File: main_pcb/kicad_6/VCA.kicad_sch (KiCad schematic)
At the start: 22 parts, among them J501 aux_AM_in, U4 TL072, U9 SSI2162

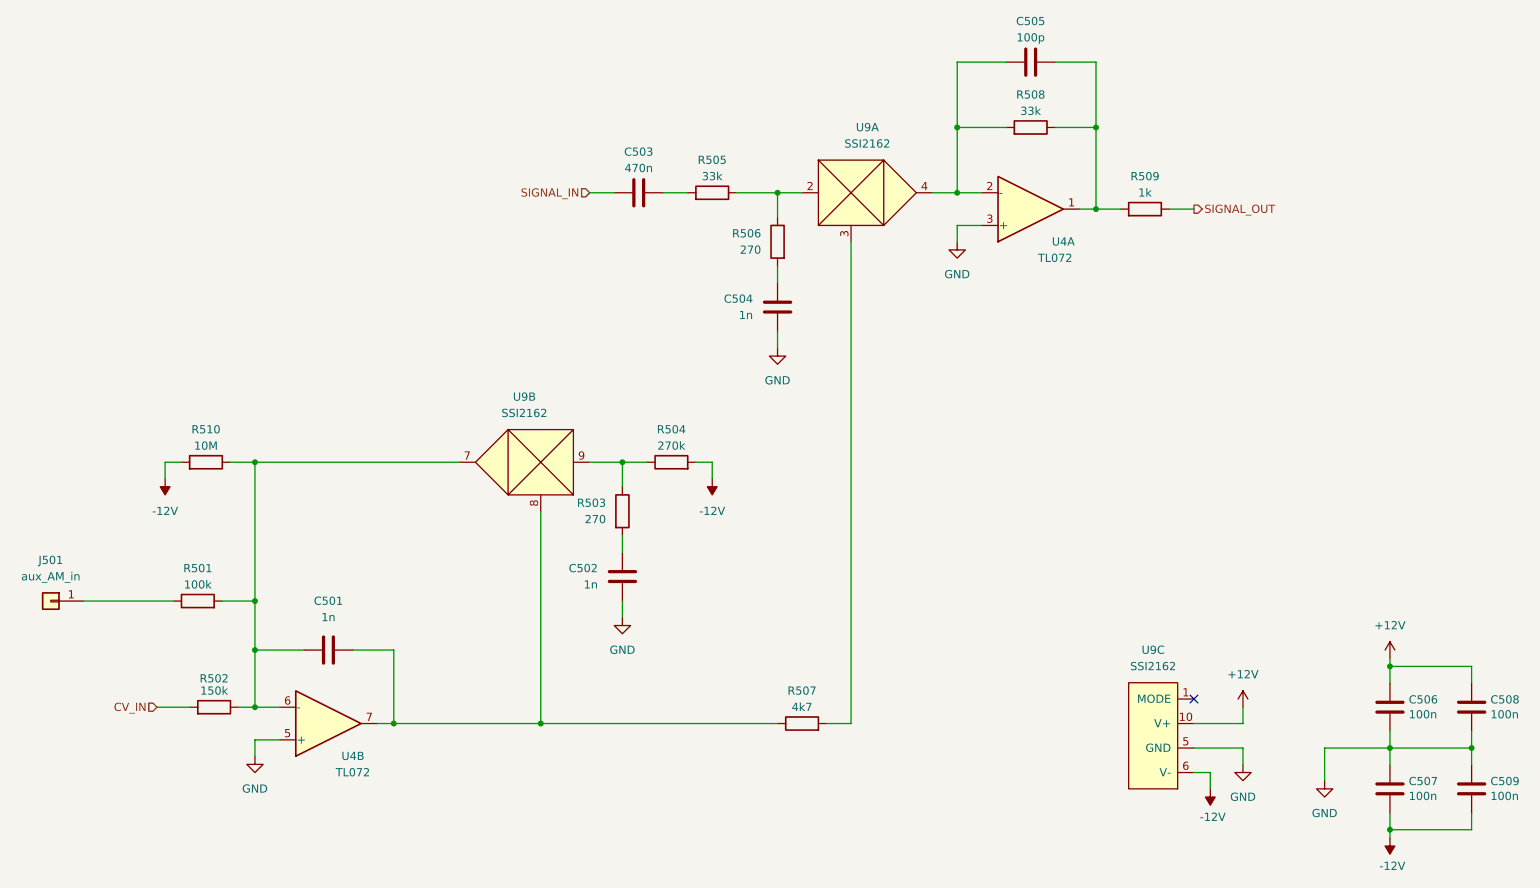
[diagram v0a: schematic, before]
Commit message: Update rev 0.1, fix VCA tails, add local 2v5 regs, change some pot footprints
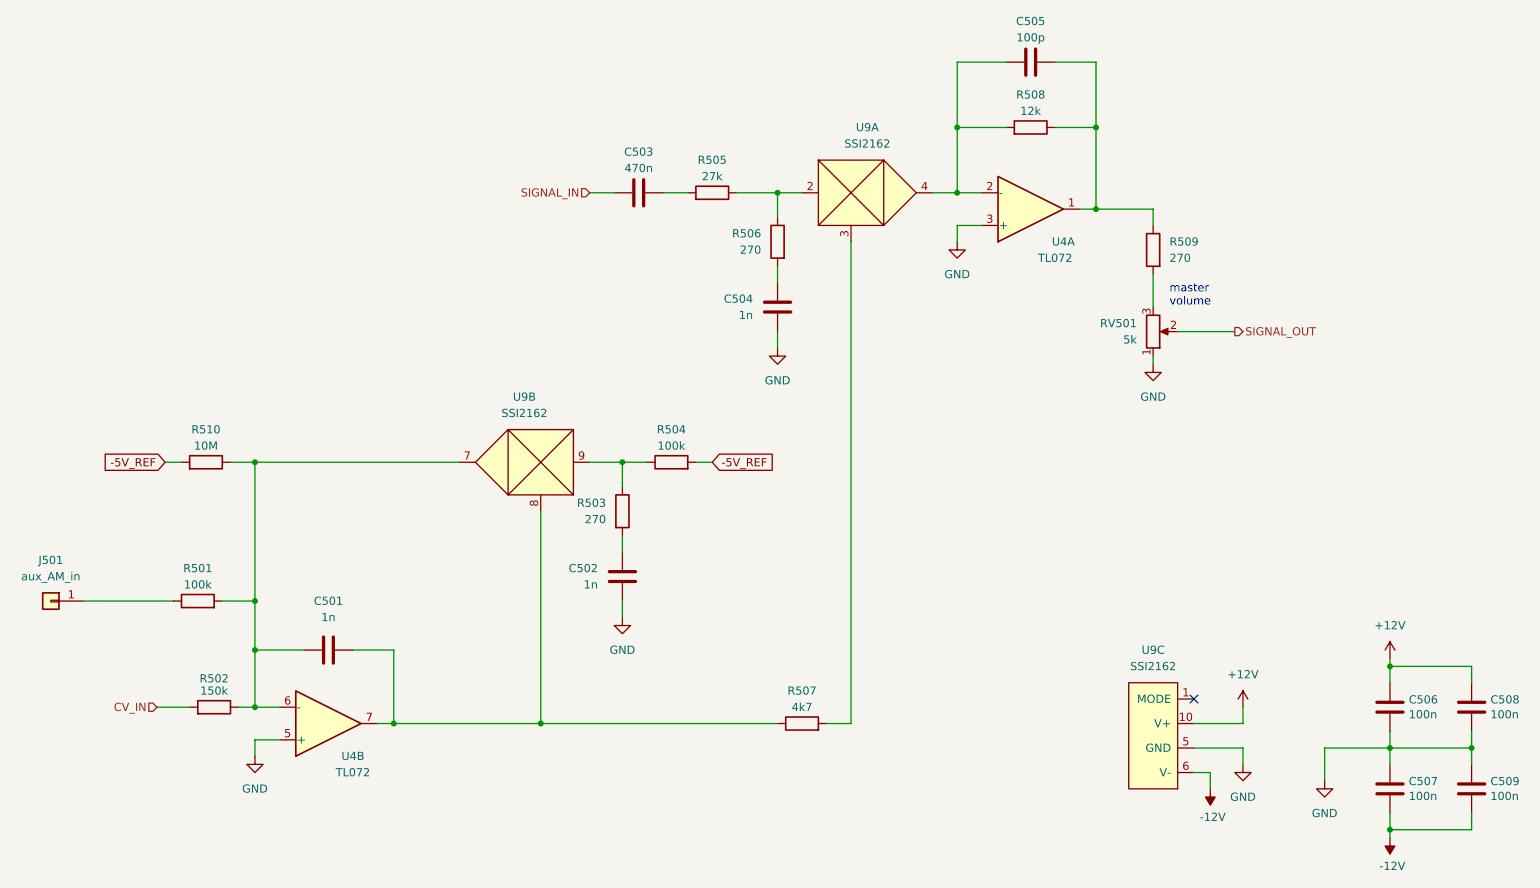
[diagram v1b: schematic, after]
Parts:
- added RV501: 5k, custom_footprints:Bourns_PTV09, symbol Device:R_Potentiometer
- J501: now left out of the parts list
- R504: value 270k -> 100k
- R505: value 33k -> 27k
- R508: value 33k -> 12k
- R509: value 1k -> 270
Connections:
- net -12V: no longer R504.2, R510.2
- net GND: now also RV501.1
- net SIGNAL_OUT: now also RV501.2; no longer R509.1
- net at C505.1, R508.1, U4.1: now also R509.1; no longer R509.2
- new net: R509.2, RV501.3
- new net -5V_REF: R504.2, R510.2
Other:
- note added: "master volume"
- moved on the sheet: R509
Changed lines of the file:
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@@
   (title_block
     (title "Micro-Pico Tiny Monosynth")
-    (date "2022-08-18")
+    (date "2022-08-28")
     (rev "0.1")
     (comment 1 "creativecommons.org/licences/by/4.0")
@@
     (stroke (width 0) (type default) (color 0 0 0 0))
   )
+  (wire (pts (xy 151.13 97.79) (xy 148.59 97.79))
+    (stroke (width 0) (type default) (color 0 0 0 0))
+  )
   (wire (pts (xy 74.93 119.38) (xy 80.01 119.38))
     (stroke (width 0) (type default) (color 0 0 0 0))
@@
     (stroke (width 0) (type default) (color 0 0 0 0))
   )
+  (wire (pts (xy 219.71 68.58) (xy 219.71 73.66))
+    (stroke (width 0) (type default) (color 0 0 0 0))
+  )
   (wire (pts (xy 137.16 97.79) (xy 140.97 97.79))
     (stroke (width 0) (type default) (color 0 0 0 0))
@@
     (stroke (width 0) (type default) (color 0 0 0 0))
   )
-  (wire (pts (xy 66.04 100.33) (xy 66.04 97.79))
-    (stroke (width 0) (type default) (color 0 0 0 0))
-  )
   (wire (pts (xy 143.51 55.88) (xy 147.32 55.88))
     (stroke (width 0) (type default) (color 0 0 0 0))
@@
     (stroke (width 0) (type default) (color 0 0 0 0))
   )
+  (wire (pts (xy 219.71 81.28) (xy 219.71 82.55))
+    (stroke (width 0) (type default) (color 0 0 0 0))
+  )
   (wire (pts (xy 137.16 101.6) (xy 137.16 97.79))
     (stroke (width 0) (type default) (color 0 0 0 0))
@@
     (stroke (width 0) (type default) (color 0 0 0 0))
   )
+  (wire (pts (xy 223.52 77.47) (xy 232.41 77.47))
+    (stroke (width 0) (type default) (color 0 0 0 0))
+  )
   (wire (pts (xy 246.38 147.32) (xy 246.38 142.24))
     (stroke (width 0) (type default) (color 0 0 0 0))
@@
     (stroke (width 0) (type default) (color 0 0 0 0))
   )
-  (wire (pts (xy 151.13 97.79) (xy 148.59 97.79))
-    (stroke (width 0) (type default) (color 0 0 0 0))
-  )
   (wire (pts (xy 226.06 142.24) (xy 233.68 142.24))
     (stroke (width 0) (type default) (color 0 0 0 0))
@@
     (stroke (width 0) (type default) (color 0 0 0 0))
   )
-  (wire (pts (xy 222.25 58.42) (xy 226.06 58.42))
-    (stroke (width 0) (type default) (color 0 0 0 0))
-  )
   (wire (pts (xy 210.82 58.42) (xy 208.28 58.42))
     (stroke (width 0) (type default) (color 0 0 0 0))
   )
-  (wire (pts (xy 214.63 58.42) (xy 210.82 58.42))
+  (wire (pts (xy 210.82 58.42) (xy 219.71 58.42))
     (stroke (width 0) (type default) (color 0 0 0 0))
   )
@@
     (stroke (width 0) (type default) (color 0 0 0 0))
   )
+  (wire (pts (xy 219.71 58.42) (xy 219.71 60.96))
+    (stroke (width 0) (type default) (color 0 0 0 0))
+  )
   (wire (pts (xy 269.24 132.08) (xy 269.24 129.54))
     (stroke (width 0) (type default) (color 0 0 0 0))
@@
     (stroke (width 0) (type default) (color 0 0 0 0))
   )
-  (wire (pts (xy 151.13 100.33) (xy 151.13 97.79))
-    (stroke (width 0) (type default) (color 0 0 0 0))
-  )
   (wire (pts (xy 124.46 138.43) (xy 161.29 138.43))
     (stroke (width 0) (type default) (color 0 0 0 0))
@@
     (stroke (width 0) (type default) (color 0 0 0 0))
   )
-  (hierarchical_label "SIGNAL_OUT" (shape output) (at 226.06 58.42 0)
+  (text "master\nvolume" (at 222.25 73.66 0)
+    (effects (font (size 1.27 1.27)) (justify left bottom))
+  )
+  (global_label "-5V_REF" (shape input) (at 66.04 97.79 180) (fields_autoplaced)
+    (effects (font (size 1.27 1.27)) (justify right))
+    (property "Intersheet References" "${INTERSHEET_REFS}" (id 0) (at 55.2812 97.8694 0)
+      (effects (font (size 1.27 1.27)) (justify right) hide)
+    )
+  )
+  (global_label "-5V_REF" (shape input) (at 151.13 97.79 0) (fields_autoplaced)
+    (effects (font (size 1.27 1.27)) (justify left))
+    (property "Intersheet References" "${INTERSHEET_REFS}" (id 0) (at 161.8888 97.7106 0)
+      (effects (font (size 1.27 1.27)) (justify left) hide)
+    )
+  )
+  (hierarchical_label "SIGNAL_OUT" (shape output) (at 232.41 77.47 0)
     (effects (font (size 1.27 1.27)) (justify left))
   )
@@
     (in_bom yes) (on_board yes)
     (property "Reference" "R504" (id 0) (at 144.78 92.71 90))
-    (property "Value" "270k" (id 1) (at 144.78 95.25 90))
+    (property "Value" "100k" (id 1) (at 144.78 95.25 90))
     (property "Footprint" "Resistor_SMD:R_0603_1608Metric" (id 2) (at 144.78 99.568 90)
       (effects (font (size 1.27 1.27)) hide)
@@
   )
   (symbol (lib_id "Connector_Generic:Conn_01x01") (at 48.26 119.38 0) (mirror y) (unit 1)
-    (in_bom yes) (on_board yes) (fields_autoplaced)
+    (in_bom no) (on_board yes) (fields_autoplaced)
     (property "Reference" "J501" (id 0) (at 48.26 113.03 0))
     (property "Value" "aux_AM_in" (id 1) (at 48.26 115.57 0))
@@
     (pin "1")
   )
+  (symbol (lib_id "Device:R_Potentiometer") (at 219.71 77.47 0) (mirror x) (unit 1)
+    (in_bom yes) (on_board yes) (fields_autoplaced)
+    (property "Reference" "RV501" (id 0) (at 217.17 76.1999 0)
+      (effects (font (size 1.27 1.27)) (justify right))
+    )
+    (property "Value" "5k" (id 1) (at 217.17 78.7399 0)
+      (effects (font (size 1.27 1.27)) (justify right))
+    )
+    (property "Footprint" "custom_footprints:Bourns_PTV09" (id 2) (at 219.71 77.47 0)
+      (effects (font (size 1.27 1.27)) hide)
+    )
+    (property "Datasheet" "~" (id 3) (at 219.71 77.47 0)
+      (effects (font (size 1.27 1.27)) hide)
+    )
+    (pin "1")
+    (pin "2")
+    (pin "3")
+  )
   (symbol (lib_id "Device:R") (at 165.1 138.43 90) (unit 1)
     (in_bom yes) (on_board yes)
@@
     (pin "1")
   )
+  (symbol (lib_id "power:GND") (at 219.71 82.55 0) (unit 1)
+    (in_bom yes) (on_board yes) (fields_autoplaced)
+    (property "Reference" "#PWR0513" (id 0) (at 219.71 88.9 0)
+      (effects (font (size 1.27 1.27)) hide)
+    )
+    (property "Value" "GND" (id 1) (at 219.71 87.63 0))
+    (property "Footprint" "" (id 2) (at 219.71 82.55 0)
+      (effects (font (size 1.27 1.27)) hide)
+    )
+    (property "Datasheet" "" (id 3) (at 219.71 82.55 0)
+      (effects (font (size 1.27 1.27)) hide)
+    )
+    (pin "1")
+  )
   (symbol (lib_id "power:GND") (at 189.23 63.5 0) (mirror y) (unit 1)
     (in_bom yes) (on_board yes) (fields_autoplaced)
@@
     (pin "1")
     (pin "2")
-  )
-  (symbol (lib_id "power:-12V") (at 151.13 100.33 0) (mirror x) (unit 1)
-    (in_bom yes) (on_board yes) (fields_autoplaced)
-    (property "Reference" "#PWR0504" (id 0) (at 151.13 102.87 0)
-      (effects (font (size 1.27 1.27)) hide)
-    )
-    (property "Value" "-12V" (id 1) (at 151.13 105.41 0))
-    (property "Footprint" "" (id 2) (at 151.13 100.33 0)
-      (effects (font (size 1.27 1.27)) hide)
-    )
-    (property "Datasheet" "" (id 3) (at 151.13 100.33 0)
-      (effects (font (size 1.27 1.27)) hide)
-    )
-    (pin "1")
-  )
-  (symbol (lib_id "power:-12V") (at 66.04 100.33 180) (unit 1)
-    (in_bom yes) (on_board yes) (fields_autoplaced)
-    (property "Reference" "#PWR0501" (id 0) (at 66.04 102.87 0)
-      (effects (font (size 1.27 1.27)) hide)
-    )
-    (property "Value" "-12V" (id 1) (at 66.04 105.41 0))
-    (property "Footprint" "" (id 2) (at 66.04 100.33 0)
-      (effects (font (size 1.27 1.27)) hide)
-    )
-    (property "Datasheet" "" (id 3) (at 66.04 100.33 0)
-      (effects (font (size 1.27 1.27)) hide)
-    )
-    (pin "1")
   )
   (symbol (lib_id "Device:C") (at 91.44 127 270) (mirror x) (unit 1)
@@
     (in_bom yes) (on_board yes)
     (property "Reference" "R505" (id 0) (at 151.13 50.8 90))
-    (property "Value" "33k" (id 1) (at 151.13 53.34 90))
+    (property "Value" "27k" (id 1) (at 151.13 53.34 90))
     (property "Footprint" "Resistor_SMD:R_0603_1608Metric" (id 2) (at 151.13 57.658 90)
       (effects (font (size 1.27 1.27)) hide)
@@
     (pin "2")
   )
-  (symbol (lib_id "Device:R") (at 218.44 58.42 270) (mirror x) (unit 1)
-    (in_bom yes) (on_board yes)
-    (property "Reference" "R509" (id 0) (at 218.44 53.34 90))
-    (property "Value" "1k" (id 1) (at 218.44 55.88 90))
-    (property "Footprint" "Resistor_SMD:R_0603_1608Metric" (id 2) (at 218.44 60.198 90)
-      (effects (font (size 1.27 1.27)) hide)
-    )
-    (property "Datasheet" "~" (id 3) (at 218.44 58.42 0)
+  (symbol (lib_id "Device:R") (at 219.71 64.77 0) (mirror y) (unit 1)
+    (in_bom yes) (on_board yes) (fields_autoplaced)
+    (property "Reference" "R509" (id 0) (at 222.25 63.4999 0)
+      (effects (font (size 1.27 1.27)) (justify right))
+    )
+    (property "Value" "270" (id 1) (at 222.25 66.0399 0)
+      (effects (font (size 1.27 1.27)) (justify right))
+    )
+    (property "Footprint" "Resistor_SMD:R_0603_1608Metric" (id 2) (at 221.488 64.77 90)
+      (effects (font (size 1.27 1.27)) hide)
+    )
+    (property "Datasheet" "~" (id 3) (at 219.71 64.77 0)
       (effects (font (size 1.27 1.27)) hide)
     )
@@
     (in_bom yes) (on_board yes)
     (property "Reference" "R508" (id 0) (at 200.66 40.64 90))
-    (property "Value" "33k" (id 1) (at 200.66 43.18 90))
+    (property "Value" "12k" (id 1) (at 200.66 43.18 90))
     (property "Footprint" "Resistor_SMD:R_0603_1608Metric" (id 2) (at 200.66 47.498 90)
       (effects (font (size 1.27 1.27)) hide)

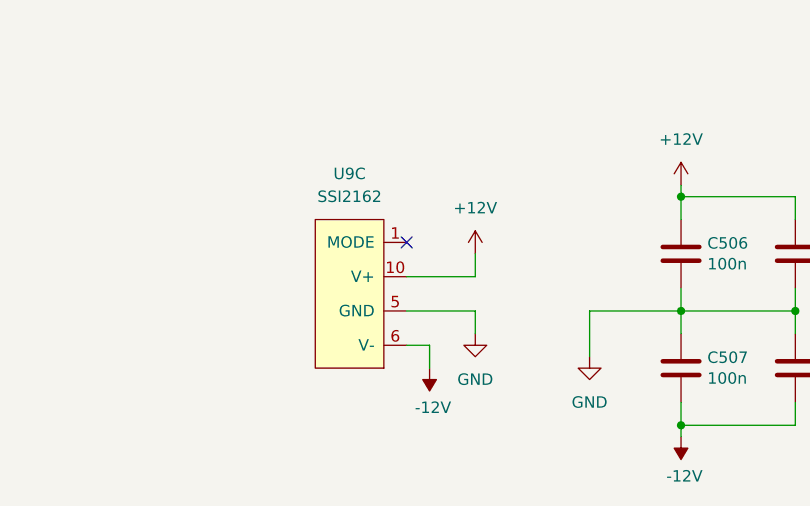
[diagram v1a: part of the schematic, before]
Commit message: Add mod-wheel VCA, fix occasional VCO freq locking
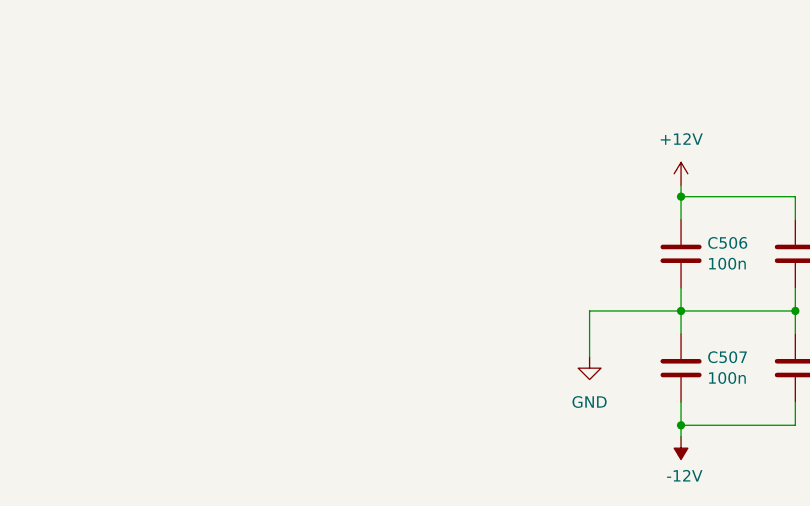
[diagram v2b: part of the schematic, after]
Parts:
- removed unit 3 of U9
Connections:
- no-connect marks 1 -> 0
